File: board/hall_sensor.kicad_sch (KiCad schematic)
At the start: 3 parts

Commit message: Connected all rows to MCPs
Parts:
- renumbered C to C23, R to R23, U to U23

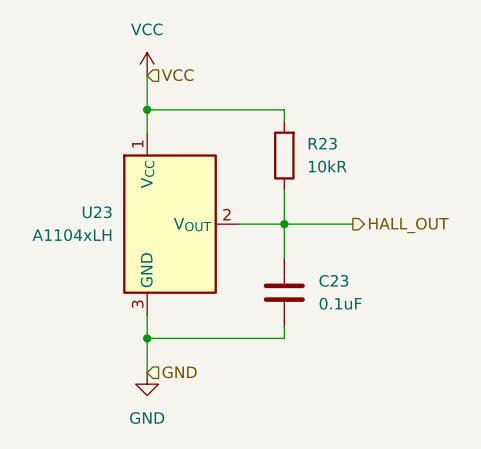
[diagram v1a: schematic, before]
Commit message: connected all sensors to mcps and all mcps to rpi4
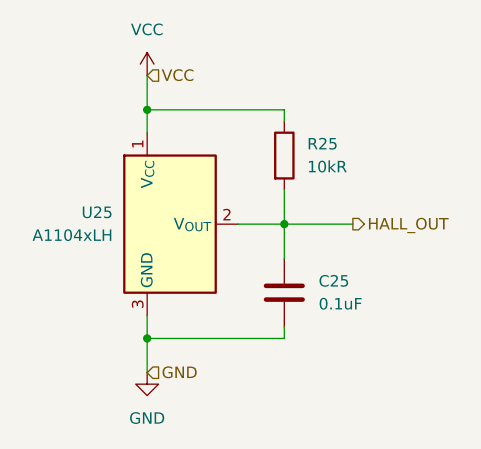
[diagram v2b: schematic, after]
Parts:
- removed C23: 0.1uF, symbol Device:C
- removed R23: 10kR, Resistor_SMD:R_0805_2012Metric, symbol Device:R
- removed U23: A1104xLH, Package_TO_SOT_SMD:SOT-23W, symbol Sensor_Magnetic:A1104xLH
- added C25: 0.1uF, Capacitor_SMD:C_0805_2012Metric, symbol Device:C
- added R25: 10kR, Resistor_SMD:R_0805_2012Metric, symbol Device:R
- added U25: A1104xLH, Package_TO_SOT_SMD:SOT-23W, symbol Sensor_Magnetic:A1104xLH
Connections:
- net GND: now also C25.2, U25.3 (GND)
- net HALL_OUT: now also C25.1, R25.2, U25.2 (V_{OUT})
- net VCC: now also R25.1, U25.1 (V_{CC})
